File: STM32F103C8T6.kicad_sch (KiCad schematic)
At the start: 51 parts, among them J1 USB_Device, J2 USB_TTL, P1 L-Pin, P2 R-Pin, P3 DEBUG, SW1 NRST, U1 MIC5219-3.3YM5, U2 CH340E, U3 STM32F103C8Tx, Y1 8MHz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

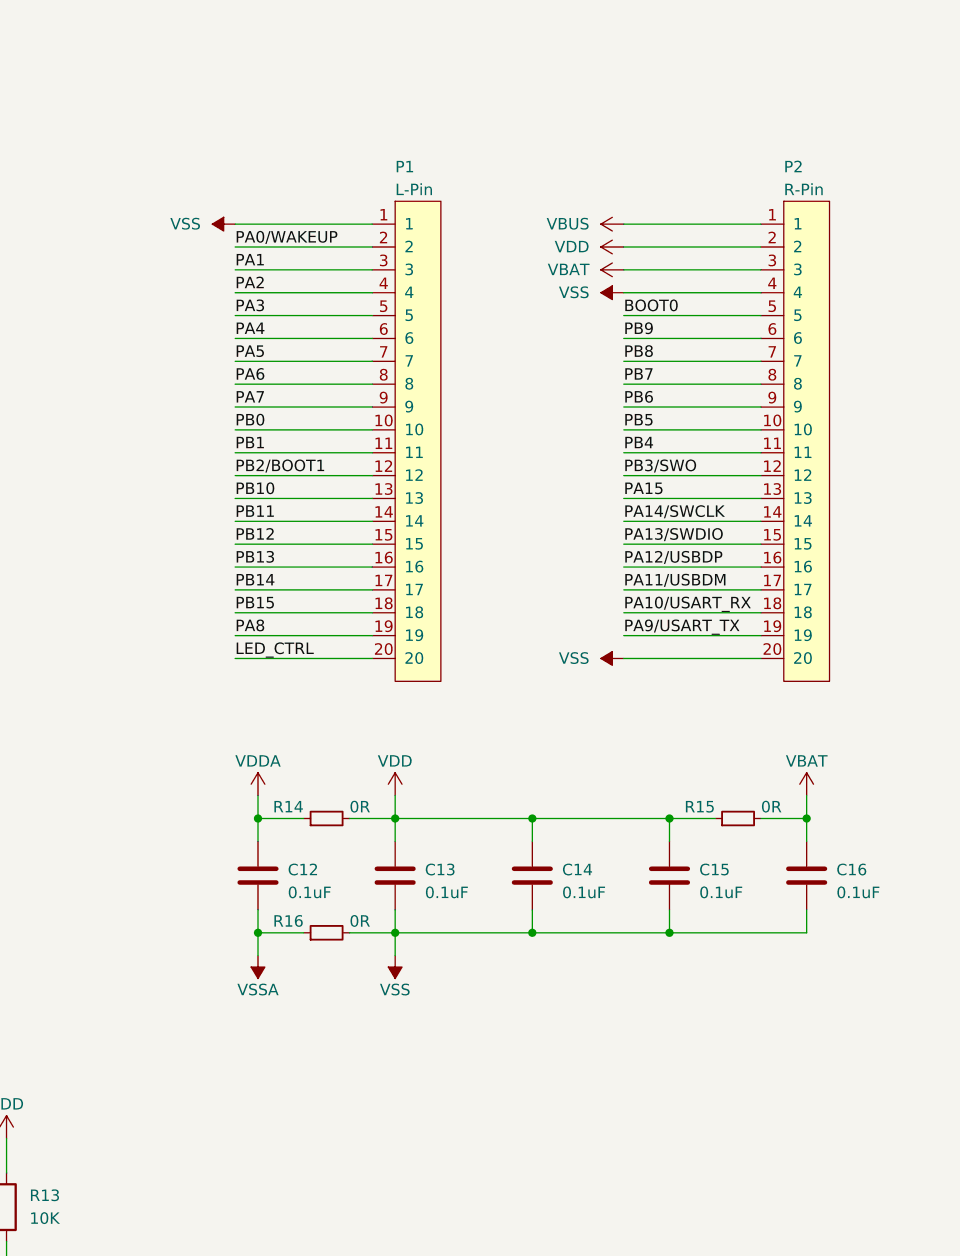
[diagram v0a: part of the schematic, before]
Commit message: 增加独立的电源连接端子
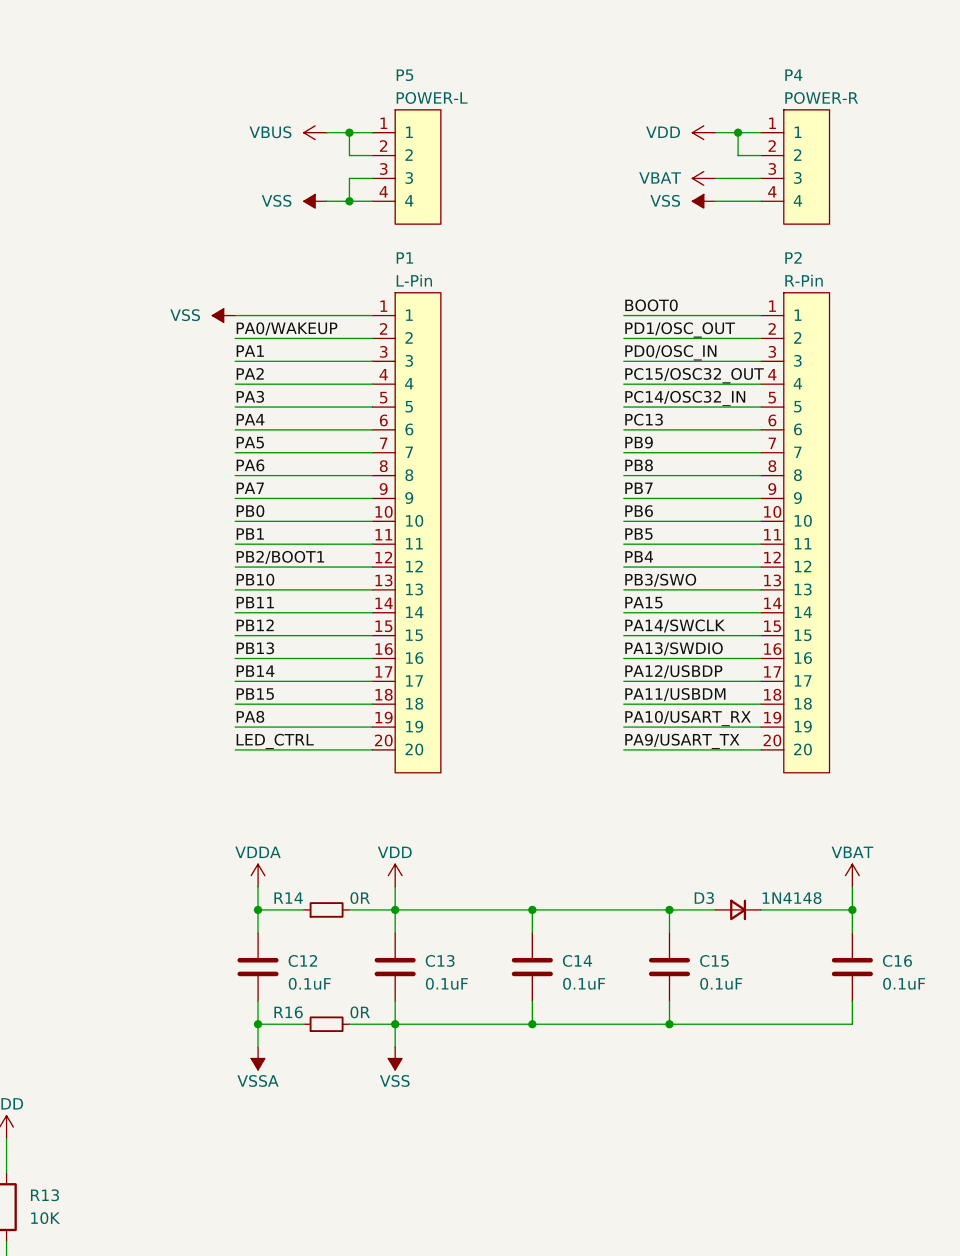
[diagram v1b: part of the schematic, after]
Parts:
- removed R15: 0R, Resistor_SMD:R_0603_1608Metric, symbol Device:R_Small
- added D3: 1N4148, Diode_SMD:D_0603_1608Metric, symbol Device:D_Small
- added P4: POWER-R, Append_Connector:HDR1×4_2.54mm, symbol Append_Connector:HEADER-1×4P
- added P5: POWER-L, Append_Connector:HDR1×4_2.54mm, symbol Append_Connector:HEADER-1×4P
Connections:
- net BOOT0: now also P2.1; no longer P2.5
- net PA10/USART_RX: now also P2.19; no longer P2.18
- net PA11/USBDM: now also P2.18; no longer P2.17
- net PA12/USBDP: now also P2.17; no longer P2.16
- net PA13/SWDIO: now also P2.16; no longer P2.15
- net PA14/SWCLK: now also P2.15; no longer P2.14
- net PA15: now also P2.14; no longer P2.13
- net PA9/USART_TX: now also P2.20; no longer P2.19
- net PB3/SWO: now also P2.13; no longer P2.12
- net PB4: now also P2.12; no longer P2.11
- net PB5: now also P2.11; no longer P2.10
- net PB6: now also P2.10; no longer P2.9
- net PB7: now also P2.9; no longer P2.8
- net PB8: now also P2.8; no longer P2.7
- net PB9: now also P2.7; no longer P2.6
- net PC13: now also P2.6
- net PC14/OSC32_IN: now also P2.5
- net PC15/OSC32_OUT: now also P2.4
- net PD0/OSC_IN: now also P2.3
- net PD1/OSC_OUT: now also P2.2
- net VBAT: now also D3.1 (K), P4.3; no longer P2.3
- net VBUS: now also P5.1, P5.2; no longer P2.1
- net VDD: now also D3.2 (A), P4.1, P4.2; no longer P2.2
- net VSS: now also P4.4, P5.3, P5.4; no longer P2.20, P2.4
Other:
- moved on the sheet: C12, C13, C14, C15, C16, P1, P2, R14, R16

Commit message: 更新电路设计，兼容F401CC芯片
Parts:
- removed U3: STM32F103C8Tx, Package_QFP:LQFP-48_7x7mm_P0.5mm, symbol MCU_ST_STM32F1:STM32F103C8Tx
- added C17: 2.2uF, Capacitor_SMD:C_0603_1608Metric, symbol Device:C
- added R15: 0R, Resistor_SMD:R_0603_1608Metric, symbol Device:R_Small
- added U3: F103C8_Class, Package_QFP:LQFP-48_7x7mm_P0.5mm, symbol Append_MCU_SOC_FPGA:F103C8_Class
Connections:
- net BOOT0: now also U3.44 (BOOT0)
- net NRST: now also U3.7 (NRST)
- net PA0/WAKEUP: now also U3.10 (PA0)
- net PA1: now also U3.11 (PA1)
- net PA10/USART_RX: now also U3.31 (PA10)
- net PA11/USBDM: now also U3.32 (PA11)
- net PA12/USBDP: now also U3.33 (PA12)
- net PA13/SWDIO: now also U3.34 (PA13)
- net PA14/SWCLK: now also U3.37 (PA14)
- net PA15: now also U3.38 (PA15)
- net PA2: now also U3.12 (PA2)
- net PA3: now also U3.13 (PA3)
- net PA4: now also U3.14 (PA4)
- net PA5: now also U3.15 (PA5)
- net PA6: now also U3.16 (PA6)
- net PA7: now also U3.17 (PA7)
- net PA8: now also U3.29 (PA8)
- net PA9/USART_TX: now also U3.30 (PA9)
- net PB0: now also U3.18 (PB0)
- net PB1: now also U3.19 (PB1)
- net PB10: now also U3.21 (PB10)
- net PB11: now also R15.1
- net PB12: now also U3.25 (PB12)
- net PB13: now also U3.26 (PB13)
- net PB14: now also U3.27 (PB14)
- net PB15: now also U3.28 (PB15)
- net PB2/BOOT1: now also U3.20 (PB2)
- net PB3/SWO: now also U3.39 (PB3)
- net PB4: now also U3.40 (PB4)
- net PB5: now also U3.41 (PB5)
- net PB6: now also U3.42 (PB6)
- net PB7: now also U3.43 (PB7)
- net PB8: now also U3.45 (PB8)
- net PB9: now also U3.46 (PB9)
- net PC13: now also U3.2 (PC13)
- net PC14/OSC32_IN: now also U3.3 (PC14)
- net PC15/OSC32_OUT: now also U3.4 (PC15)
- net PD0/OSC_IN: now also U3.5 (PD0)
- net PD1/OSC_OUT: now also U3.6 (PD1)
- net VBAT: now also U3.1 (VBAT)
- net VDD: now also U3.24 (VDD), U3.36 (VDD/PF5), U3.48 (VDD); no longer C15.1
- net VDDA: now also U3.9 (VDDA)
- net VSS: now also C15.1, C17.1, U3.23 (VSS), U3.35 (VSS/PF6), U3.47 (VSS), U3.49 (VSS)
- net VSSA: now also U3.8 (VSSA)
- new net VCAP: C17.2, R15.2, U3.22 (PB11/VCAP)
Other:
- moved on the sheet: C15

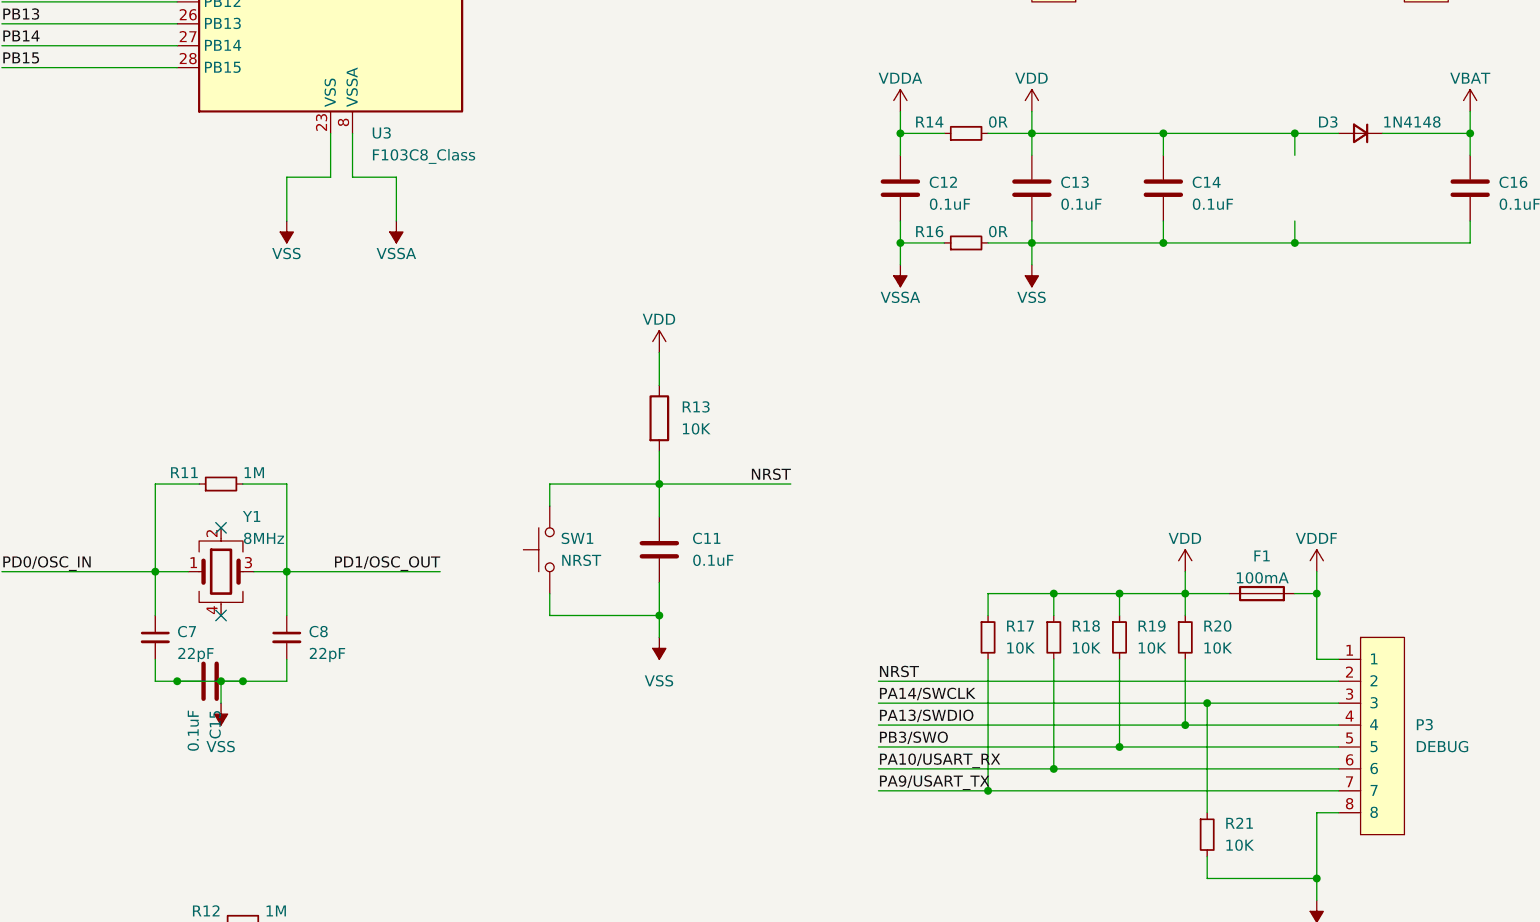
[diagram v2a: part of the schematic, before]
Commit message: 优化电源走线
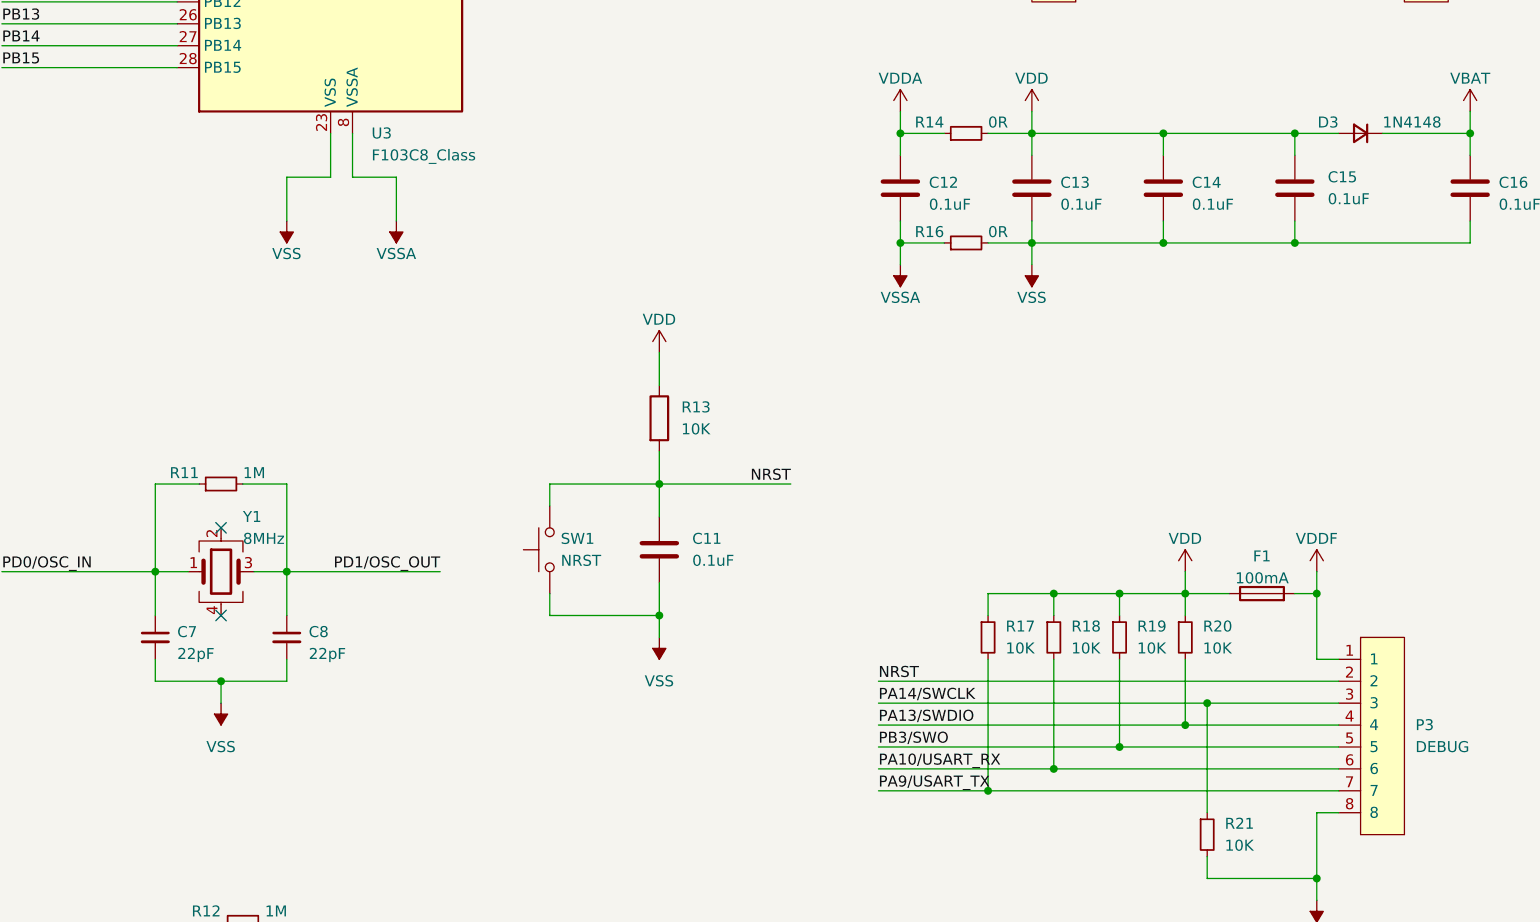
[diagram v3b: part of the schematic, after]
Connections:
- net VDD: now also C15.1
- net VSS: no longer C15.1
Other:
- moved on the sheet: C15
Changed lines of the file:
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@@
 	)
 	(junction
-		(at 231.14 190.5)
-		(diameter 0)
-		(color 0 0 0 0)
-	)
-	(junction
-		(at 223.52 190.5)
-		(diameter 0)
-		(color 0 0 0 0)
-	)
-	(junction
 		(at 353.06 139.7)
 		(diameter 0)
@@
 	(wire
 		(pts
-			(xy 228.6 190.5) (xy 223.52 190.5)
-		)
-		(stroke
-			(width 0)
-			(type default)
-		)
-	)
-	(wire
-		(pts
 			(xy 322.58 139.7) (xy 322.58 142.24)
 		)
@@
 	(wire
 		(pts
-			(xy 223.52 190.5) (xy 220.98 190.5)
+			(xy 220.98 190.5) (xy 228.6 190.5)
 		)
 		(stroke
@@
 	(wire
 		(pts
-			(xy 231.14 190.5) (xy 228.6 190.5)
+			(xy 228.6 190.5) (xy 236.22 190.5)
 		)
 		(stroke
@@
 	(wire
 		(pts
-			(xy 236.22 190.5) (xy 231.14 190.5)
-		)
-		(stroke
-			(width 0)
-			(type default)
-		)
-	)
-	(wire
-		(pts
 			(xy 342.9 213.36) (xy 355.6 213.36)
 		)
@@
 	(symbol
 		(lib_id "Device:C")
-		(at 227.33 190.5 270)
+		(at 353.06 133.35 0)
 		(unit 1)
 		(exclude_from_sim no)
@@
 		(fields_autoplaced yes)
 		(property "Reference" "C15"
-			(at 227.965 193.802 0)
+			(at 356.87 132.0799 0)
 			(effects
 				(font
@@
 		)
 		(property "Value" "0.1uF"
-			(at 225.425 193.802 0)
+			(at 356.87 134.6199 0)
 			(effects
 				(font
@@
 		)
 		(property "Footprint" "Capacitor_SMD:C_0603_1608Metric"
-			(at 223.52 191.4652 0)
+			(at 354.0252 137.16 0)
 			(effects
 				(font
@@
 		)
 		(property "Datasheet" "~"
-			(at 227.33 190.5 0)
+			(at 353.06 133.35 0)
 			(effects
 				(font
@@
 		)
 		(property "Description" ""
-			(at 227.33 190.5 0)
+			(at 353.06 133.35 0)
 			(effects
 				(font
